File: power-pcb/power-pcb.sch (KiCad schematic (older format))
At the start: 6 parts, among them CON101 10118194-0001LF, CON102 HDR1X2, CON103 GENESIS-CONN, CON104 SMS-CONN

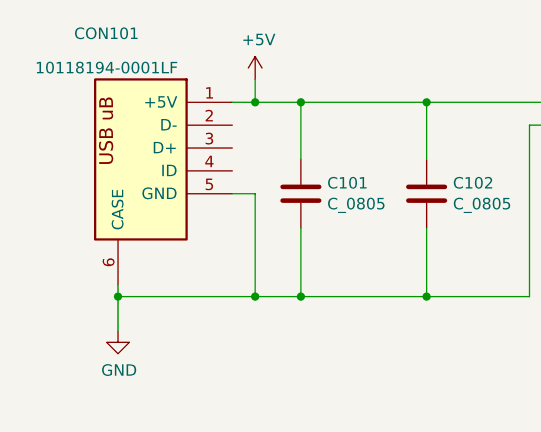
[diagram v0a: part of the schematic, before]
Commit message: changed USB conn
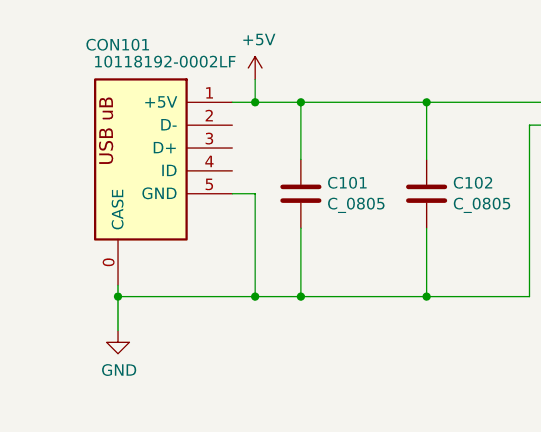
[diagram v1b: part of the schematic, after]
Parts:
- removed CON101: 10118194-0001LF, db-smt:USB-uB-10118194, symbol db-connectors:10118194-0001LF
- added CON101: 10118192-0002LF, db-smt:USB-10118192-0002, symbol db-connectors:10118192-0002LF
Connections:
- net +5V: now also CON101.1 (+5V)
- net GND: now also CON101.0 (CASE), CON101.5 (GND)
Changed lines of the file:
@@
 EESchema Schematic File Version 4
+LIBS:power-pcb-cache
 EELAYER 26 0
 EELAYER END
@@
 $EndDescr
 $Comp
-L db-connectors:10118194-0001LF CON101
-U 1 1 5BEEF85E
-P 2550 2200
-F 0 "CON101" H 2900 2400 50  0000 C CNN
-F 1 "10118194-0001LF" H 2900 2250 50  0000 C CNN
-F 2 "db-smt:USB-uB-10118194" H 3175 2725 60  0001 C CNN
-F 3 "https://cdn.amphenol-icc.com/media/wysiwyg/files/drawing/10118194.pdf" H 4300 2425 60  0001 C CNN
-F 4 "609-4618-1-ND" H 2950 2625 60  0001 C CNN "Digikey"
-F 5 "CONN USB MICRO B RECPT SMT R/A" H 3375 2525 60  0001 C CNN "Description"
-	1    2550 2200
-	-1   0    0    -1
-$EndComp
-$Comp
 L db-vgparts:GENESIS-CONN CON103
 U 1 1 5BEEF8BA
@@
 Wire Wire Line
 	3600 3150 3050 3150
+$Comp
+L db-connectors:10118192-0002LF CON101
+U 1 1 5BF4018D
+P 2550 2200
+F 0 "CON101" H 2850 2350 50  0000 C CNN
+F 1 "10118192-0002LF" H 2645 2276 50  0000 C CNN
+F 2 "db-smt:USB-10118192-0002" H 3250 2700 60  0001 C CNN
+F 3 "https://cdn.amphenol-icc.com/media/wysiwyg/files/drawing/10118194.pdf" H 4300 2425 60  0001 C CNN
+F 4 "609-5379-1-ND" H 2950 2625 60  0001 C CNN "Digikey"
+F 5 "CONN USB MICRO B RECPT SMT R/A" H 3375 2525 60  0001 C CNN "Description"
+	1    2550 2200
+	-1   0    0    -1
+$EndComp
 $EndSCHEMATC

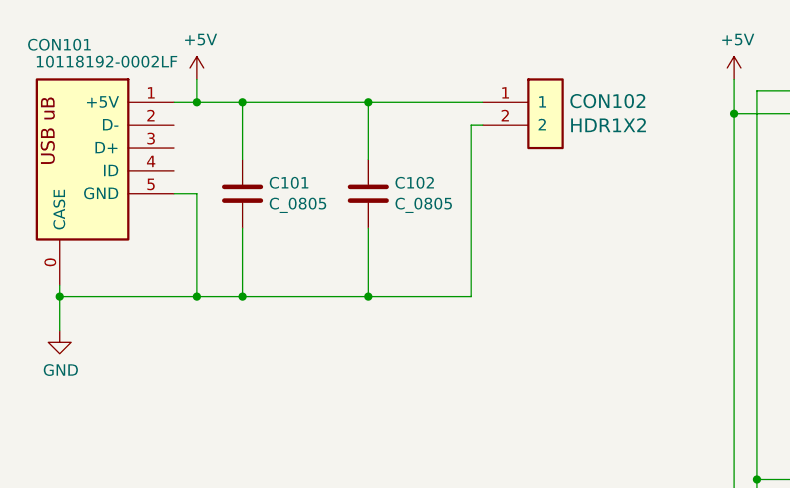
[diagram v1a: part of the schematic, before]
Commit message: added C101, C102 part numbers, added BOM and Gerbers for 0.1 release
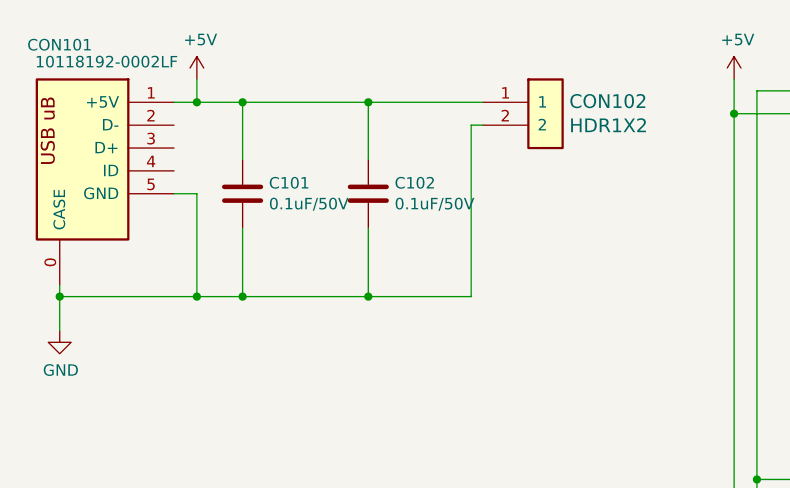
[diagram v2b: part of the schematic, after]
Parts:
- C101, C102: value C_0805 -> 0.1uF/50V; Description #ND -> CAP CER 0.1UF 50V Y5V 0805; Digikey #ND -> 1276-1007-1-ND
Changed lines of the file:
@@
 P 3050 2700
 F 0 "C101" H 3165 2746 50  0000 L CNN
-F 1 "C_0805" H 3165 2655 50  0000 L CNN
+F 1 "0.1uF/50V" H 3165 2655 50  0000 L CNN
 F 2 "db-smt:0805" H 3088 2550 30  0001 C CNN
 F 3 "" H 3075 2800 60  0000 C CNN
-F 4 "#ND" H 3175 2900 60  0001 C CNN "Digikey"
-F 5 "#ND" H 3175 3000 60  0001 C CNN "Description"
+F 4 "1276-1007-1-ND" H 3175 2900 60  0001 C CNN "Digikey"
+F 5 "CAP CER 0.1UF 50V Y5V 0805" H 3175 3000 60  0001 C CNN "Description"
 	1    3050 2700
 	1    0    0    -1
@@
 P 3600 2700
 F 0 "C102" H 3715 2746 50  0000 L CNN
-F 1 "C_0805" H 3715 2655 50  0000 L CNN
+F 1 "0.1uF/50V" H 3715 2655 50  0000 L CNN
 F 2 "db-smt:0805" H 3638 2550 30  0001 C CNN
 F 3 "" H 3625 2800 60  0000 C CNN
-F 4 "#ND" H 3725 2900 60  0001 C CNN "Digikey"
-F 5 "#ND" H 3725 3000 60  0001 C CNN "Description"
+F 4 "1276-1007-1-ND" H 3725 2900 60  0001 C CNN "Digikey"
+F 5 "CAP CER 0.1UF 50V Y5V 0805" H 3725 3000 60  0001 C CNN "Description"
 	1    3600 2700
 	1    0    0    -1
